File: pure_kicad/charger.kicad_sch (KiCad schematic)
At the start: 43 parts, among them J1 XT60M, J2 XT60M, Q1 Q_NMOS_DGS, Q2 Q_NMOS_DGS, Q3 Q_NMOS_DGS, Q4 Q_NMOS_DGS, U1 BQ25756ERRVR

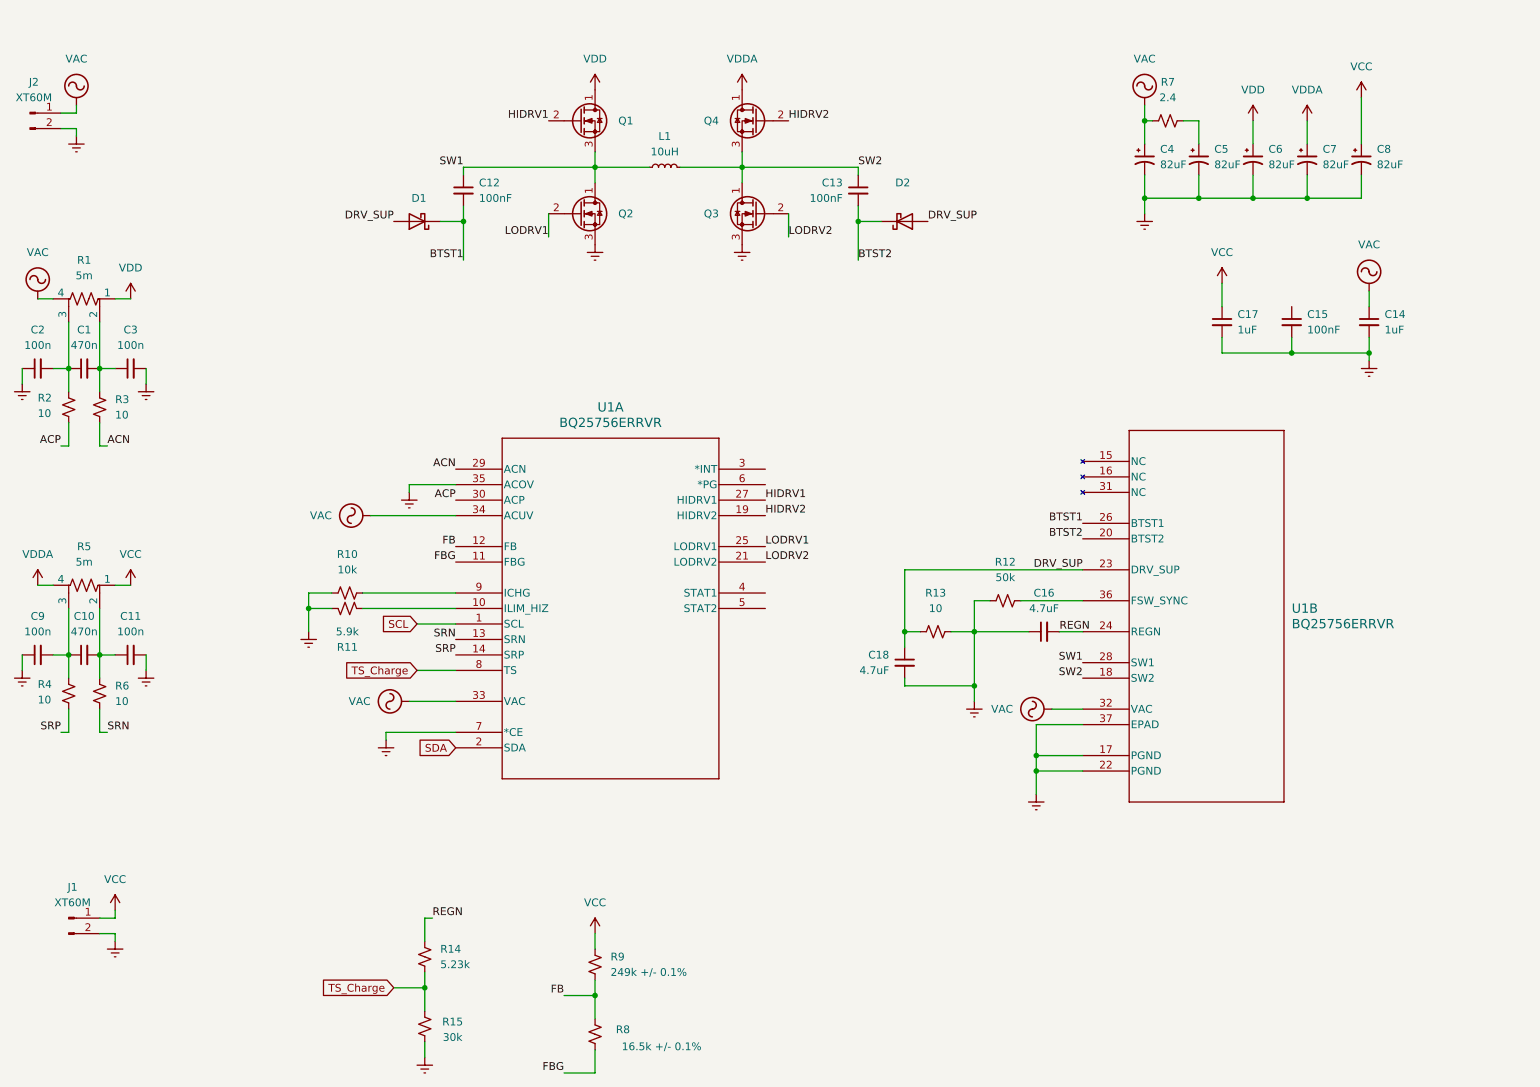
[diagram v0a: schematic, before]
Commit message: Assign parts, start layout
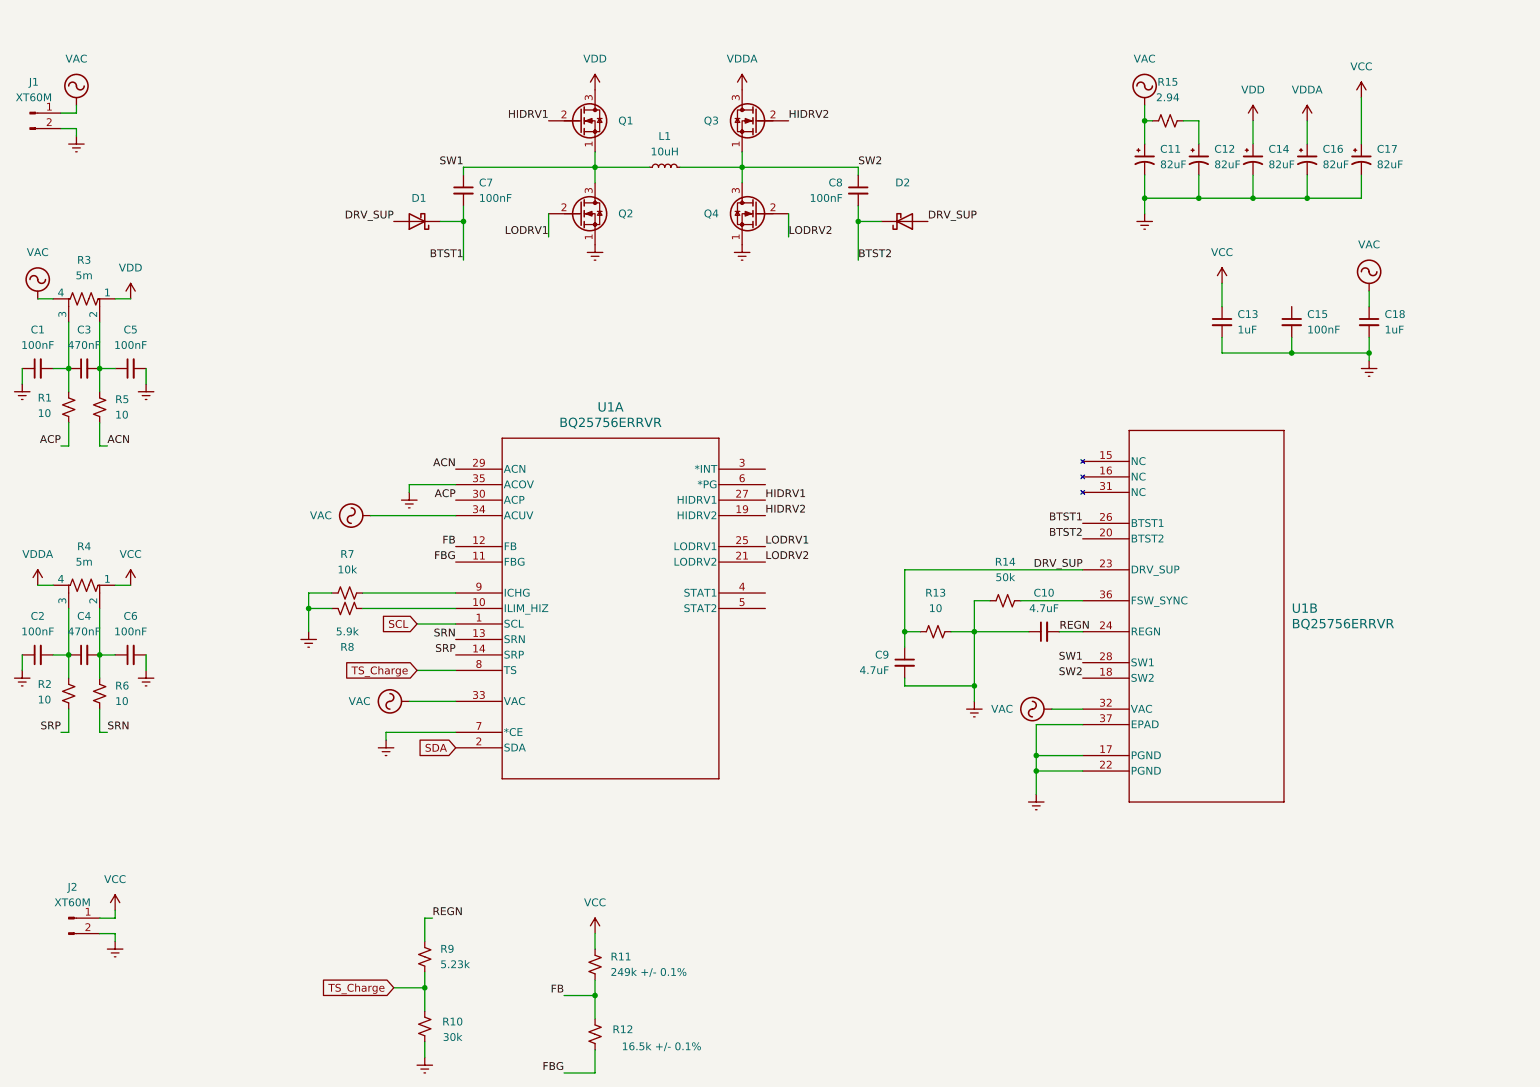
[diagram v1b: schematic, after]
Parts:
- C1: renamed from C2; value 100n -> 100nF; footprint Capacitor_SMD:C_0402_1005Metric_Pad0.74x0.62mm_HandSolder -> Capacitor_SMD:C_0603_1608Metric_Pad1.08x0.95mm_HandSolder
- C10: renamed from C16; footprint Capacitor_SMD:C_0402_1005Metric_Pad0.74x0.62mm_HandSolder -> Capacitor_SMD:C_0603_1608Metric_Pad1.08x0.95mm_HandSolder
- C11: renamed from C4; footprint (none) -> Capacitor_SMD:CP_Elec_10x14.3
- C12: renamed from C5; footprint (none) -> Capacitor_SMD:CP_Elec_10x14.3
- C13: renamed from C17; footprint (none) -> Capacitor_SMD:C_0603_1608Metric_Pad1.08x0.95mm_HandSolder
- C14: renamed from C6; footprint (none) -> Capacitor_SMD:CP_Elec_10x14.3
- C15: footprint (none) -> Capacitor_SMD:C_0603_1608Metric_Pad1.08x0.95mm_HandSolder
- C16: renamed from C7; footprint (none) -> Capacitor_SMD:CP_Elec_10x14.3
- C17: renamed from C8; footprint (none) -> Capacitor_SMD:CP_Elec_10x14.3
- C18: renamed from C14; footprint (none) -> Capacitor_SMD:C_0603_1608Metric_Pad1.08x0.95mm_HandSolder
- C2: renamed from C9; value 100n -> 100nF; footprint Capacitor_SMD:C_0402_1005Metric_Pad0.74x0.62mm_HandSolder -> Capacitor_SMD:C_0603_1608Metric_Pad1.08x0.95mm_HandSolder
- C3: renamed from C1; value 470n -> 470nF; footprint Capacitor_SMD:C_0402_1005Metric_Pad0.74x0.62mm_HandSolder -> Capacitor_SMD:C_0603_1608Metric_Pad1.08x0.95mm_HandSolder
- C4: renamed from C10; value 470n -> 470nF; footprint Capacitor_SMD:C_0402_1005Metric_Pad0.74x0.62mm_HandSolder -> Capacitor_SMD:C_0603_1608Metric_Pad1.08x0.95mm_HandSolder
- C5: renamed from C3; value 100n -> 100nF; footprint Capacitor_SMD:C_0402_1005Metric_Pad0.74x0.62mm_HandSolder -> Capacitor_SMD:C_0603_1608Metric_Pad1.08x0.95mm_HandSolder
- C6: renamed from C11; value 100n -> 100nF; footprint Capacitor_SMD:C_0402_1005Metric_Pad0.74x0.62mm_HandSolder -> Capacitor_SMD:C_0603_1608Metric_Pad1.08x0.95mm_HandSolder
- C7: renamed from C12; footprint (none) -> Capacitor_SMD:C_0603_1608Metric_Pad1.08x0.95mm_HandSolder
- C8: renamed from C13; footprint (none) -> Capacitor_SMD:C_0603_1608Metric_Pad1.08x0.95mm_HandSolder
- C9: renamed from C18; footprint Capacitor_SMD:C_0402_1005Metric_Pad0.74x0.62mm_HandSolder -> Capacitor_SMD:C_0603_1608Metric_Pad1.08x0.95mm_HandSolder
- D1, D2: footprint (none) -> Diode_SMD:D_SMA_Handsoldering
- L1: footprint (none) -> cyberec:IND-SMD_L13.5-W12.6
- Q1, Q2: footprint (none) -> cyberec:DFN-8_L3.0-W3.0-P0.65-BL-4; symbol Transistor_FET:Q_NMOS_DGS -> Transistor_FET:Q_NMOS_SGD
- Q3: renamed from Q4; footprint (none) -> cyberec:DFN-8_L3.0-W3.0-P0.65-BL-4; symbol Transistor_FET:Q_NMOS_DGS -> Transistor_FET:Q_NMOS_SGD
- Q4: renamed from Q3; footprint (none) -> cyberec:DFN-8_L3.0-W3.0-P0.65-BL-4; symbol Transistor_FET:Q_NMOS_DGS -> Transistor_FET:Q_NMOS_SGD
- R1: renamed from R2; footprint Resistor_SMD:R_0402_1005Metric_Pad0.72x0.64mm_HandSolder -> Resistor_SMD:R_0603_1608Metric_Pad0.98x0.95mm_HandSolder
- R10: renamed from R15; footprint Resistor_SMD:R_0402_1005Metric_Pad0.72x0.64mm_HandSolder -> Resistor_SMD:R_0603_1608Metric_Pad0.98x0.95mm_HandSolder
- R11: renamed from R9; footprint Resistor_SMD:R_0402_1005Metric_Pad0.72x0.64mm_HandSolder -> Resistor_SMD:R_0603_1608Metric_Pad0.98x0.95mm_HandSolder
- R12: renamed from R8; footprint Resistor_SMD:R_0402_1005Metric_Pad0.72x0.64mm_HandSolder -> Resistor_SMD:R_0603_1608Metric_Pad0.98x0.95mm_HandSolder
- R13, R6: footprint Resistor_SMD:R_0402_1005Metric_Pad0.72x0.64mm_HandSolder -> Resistor_SMD:R_0603_1608Metric_Pad0.98x0.95mm_HandSolder
- R15: renamed from R7; value 2.4 -> 2.94; footprint (none) -> Resistor_SMD:R_0603_1608Metric_Pad0.98x0.95mm_HandSolder
- R2: renamed from R4; footprint Resistor_SMD:R_0402_1005Metric_Pad0.72x0.64mm_HandSolder -> Resistor_SMD:R_0603_1608Metric_Pad0.98x0.95mm_HandSolder
- R3: renamed from R1; footprint (none) -> cyberec:R1206-sense-handsolder
- R4: renamed from R5; footprint (none) -> cyberec:R1206-sense-handsolder
- R5: renamed from R3; footprint Resistor_SMD:R_0402_1005Metric_Pad0.72x0.64mm_HandSolder -> Resistor_SMD:R_0603_1608Metric_Pad0.98x0.95mm_HandSolder
- R7: renamed from R10; footprint Resistor_SMD:R_0402_1005Metric_Pad0.72x0.64mm_HandSolder -> Resistor_SMD:R_0603_1608Metric_Pad0.98x0.95mm_HandSolder
- R8: renamed from R11; footprint Resistor_SMD:R_0402_1005Metric_Pad0.72x0.64mm_HandSolder -> Resistor_SMD:R_0603_1608Metric_Pad0.98x0.95mm_HandSolder
- R9: renamed from R14; footprint Resistor_SMD:R_0402_1005Metric_Pad0.72x0.64mm_HandSolder -> Resistor_SMD:R_0603_1608Metric_Pad0.98x0.95mm_HandSolder
- renumbered J2 to J1, J1 to J2, R12 to R14
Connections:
- net Earth: now also Q2.1 (S), Q4.1 (S); no longer Q2.3 (S), Q4.3 (S)
- net SW1: now also Q1.1 (S), Q2.3 (D); no longer Q1.3 (S), Q2.1 (D)
- net SW2: now also Q3.1 (S), Q4.3 (D); no longer Q3.3 (S), Q4.1 (D)
- net VDD: now also Q1.3 (D); no longer Q1.1 (D)
- net VDDA: now also Q3.3 (D); no longer Q3.1 (D)

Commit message: Layout starting to look alright
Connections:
- net VAC: now also C15.1
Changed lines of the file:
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@@
+	)
+	(junction
+		(at 256.54 63.5)
+		(diameter 0)
+		(color 0 0 0 0)
 	)
 	(junction
@@
 	(wire
 		(pts
+			(xy 256.54 63.5) (xy 256.54 64.77)
+		)
+		(stroke
+			(width 0)
+			(type default)
+		)
+	)
+	(wire
+		(pts
 			(xy 129.54 41.91) (xy 138.43 41.91)
 		)
@@
 	(wire
 		(pts
-			(xy 256.54 62.23) (xy 256.54 64.77)
+			(xy 256.54 62.23) (xy 256.54 63.5)
 		)
 		(stroke
@@
 	(wire
 		(pts
+			(xy 243.84 63.5) (xy 256.54 63.5)
+		)
+		(stroke
+			(width 0)
+			(type default)
+		)
+	)
+	(wire
+		(pts
 			(xy 40.64 74.93) (xy 43.18 74.93)
 		)
@@
 		)
 		(stroke
+			(width 0)
+			(type default)
+		)
+	)
+	(wire
+		(pts
+			(xy 243.84 64.77) (xy 243.84 63.5)
+		)
+		(stroke

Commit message: Import all the footprints, use project local 3d files
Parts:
- C1, C10, C13, C15, C18, C2, C3, C4, C5, C6, C7, C8, C9: footprint Capacitor_SMD:C_0603_1608Metric_Pad1.08x0.95mm_HandSolder -> cyberec:C_0603_1608Metric_Pad1.08x0.95mm_HandSolder
- C11, C12, C14, C16, C17: footprint Capacitor_SMD:CP_Elec_10x14.3 -> cyberec:CP_Elec_10x14.3
- D1, D2: footprint Diode_SMD:D_SMA_Handsoldering -> cyberec:D_SMA_Handsoldering
- J1, J2: footprint Connector_AMASS:AMASS_XT60-M_1x02_P7.20mm_Vertical -> cyberec:AMASS_XT60-M_1x02_P7.20mm_Vertical
- R1, R10, R11, R12, R13, R15, R2, R5, R6, R7, R8, R9: footprint Resistor_SMD:R_0603_1608Metric_Pad0.98x0.95mm_HandSolder -> cyberec:R_0603_1608Metric_Pad0.98x0.95mm_HandSolder
- R14: footprint Resistor_SMD:R_0402_1005Metric_Pad0.72x0.64mm_HandSolder -> cyberec:R_0402_1005Metric_Pad0.72x0.64mm_HandSolder
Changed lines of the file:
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@@
 			)
 		)
-		(property "Footprint" "Resistor_SMD:R_0603_1608Metric_Pad0.98x0.95mm_HandSolder"
+		(property "Footprint" "cyberec:R_0603_1608Metric_Pad0.98x0.95mm_HandSolder"
 			(at 185.42 118.11 0)
 			(effects
@@
 			)
 		)
-		(property "Footprint" "Capacitor_SMD:C_0603_1608Metric_Pad1.08x0.95mm_HandSolder"
+		(property "Footprint" "cyberec:C_0603_1608Metric_Pad1.08x0.95mm_HandSolder"
 			(at 38.1 121.92 0)
 			(effects
@@
 			)
 		)
-		(property "Footprint" "Capacitor_SMD:CP_Elec_10x14.3"
+		(property "Footprint" "cyberec:CP_Elec_10x14.3"
 			(at 246.38 40.64 0)
 			(effects
@@
 			)
 		)
-		(property "Footprint" "Diode_SMD:D_SMA_Handsoldering"
+		(property "Footprint" "cyberec:D_SMA_Handsoldering"
 			(at 100.33 50.8 0)
 			(effects
@@
 			)
 		)
-		(property "Footprint" "Capacitor_SMD:C_0603_1608Metric_Pad1.08x0.95mm_HandSolder"
+		(property "Footprint" "cyberec:C_0603_1608Metric_Pad1.08x0.95mm_HandSolder"
 			(at 107.95 45.72 0)
 			(effects
@@
 			)
 		)
-		(property "Footprint" "Resistor_SMD:R_0603_1608Metric_Pad0.98x0.95mm_HandSolder"
+		(property "Footprint" "cyberec:R_0603_1608Metric_Pad0.98x0.95mm_HandSolder"
 			(at 43.18 81.28 0)
 			(effects
@@
 			)
 		)
-		(property "Footprint" "Capacitor_SMD:CP_Elec_10x14.3"
+		(property "Footprint" "cyberec:CP_Elec_10x14.3"
 			(at 219.71 40.64 0)
 			(effects
@@
 			)
 		)
-		(property "Footprint" "Capacitor_SMD:CP_Elec_10x14.3"
+		(property "Footprint" "cyberec:CP_Elec_10x14.3"
 			(at 237.49 40.64 0)
 			(effects
@@
 			)
 		)
-		(property "Footprint" "Resistor_SMD:R_0603_1608Metric_Pad0.98x0.95mm_HandSolder"
+		(property "Footprint" "cyberec:R_0603_1608Metric_Pad0.98x0.95mm_HandSolder"
 			(at 48.26 128.27 0)
 			(effects
@@
 			)
 		)
-		(property "Footprint" "Capacitor_SMD:C_0603_1608Metric_Pad1.08x0.95mm_HandSolder"
+		(property "Footprint" "cyberec:C_0603_1608Metric_Pad1.08x0.95mm_HandSolder"
 			(at 180.34 123.19 0)
 			(effects
@@
 			)
 		)
-		(property "Footprint" "Resistor_SMD:R_0603_1608Metric_Pad0.98x0.95mm_HandSolder"
+		(property "Footprint" "cyberec:R_0603_1608Metric_Pad0.98x0.95mm_HandSolder"
 			(at 129.54 184.15 0)
 			(effects
@@
 			)
 		)
-		(property "Footprint" "Resistor_SMD:R_0603_1608Metric_Pad0.98x0.95mm_HandSolder"
+		(property "Footprint" "cyberec:R_0603_1608Metric_Pad0.98x0.95mm_HandSolder"
 			(at 101.6 182.88 0)
 			(effects
@@
 			)
 		)
-		(property "Footprint" "Connector_AMASS:AMASS_XT60-M_1x02_P7.20mm_Vertical"
+		(property "Footprint" "cyberec:AMASS_XT60-M_1x02_P7.20mm_Vertical"
 			(at 36.83 33.02 0)
 			(effects
@@
 			)
 		)
-		(property "Footprint" "Resistor_SMD:R_0603_1608Metric_Pad0.98x0.95mm_HandSolder"
+		(property "Footprint" "cyberec:R_0603_1608Metric_Pad0.98x0.95mm_HandSolder"
 			(at 223.52 34.29 0)
 			(effects
@@
 			)
 		)
-		(property "Footprint" "Capacitor_SMD:C_0603_1608Metric_Pad1.08x0.95mm_HandSolder"
+		(property "Footprint" "cyberec:C_0603_1608Metric_Pad1.08x0.95mm_HandSolder"
 			(at 45.72 121.92 0)
 			(effects
@@
 			)
 		)
-		(property "Footprint" "Capacitor_SMD:CP_Elec_10x14.3"
+		(property "Footprint" "cyberec:CP_Elec_10x14.3"
 			(at 228.6 40.64 0)
 			(effects
@@
 			)
 		)
-		(property "Footprint" "Resistor_SMD:R_0603_1608Metric_Pad0.98x0.95mm_HandSolder"
+		(property "Footprint" "cyberec:R_0603_1608Metric_Pad0.98x0.95mm_HandSolder"
 			(at 88.9 111.76 0)
 			(effects
@@
 			)
 		)
-		(property "Footprint" "Capacitor_SMD:CP_Elec_10x14.3"
+		(property "Footprint" "cyberec:CP_Elec_10x14.3"
 			(at 255.27 40.64 0)
 			(effects
@@
 			)
 		)
-		(property "Footprint" "Resistor_SMD:R_0402_1005Metric_Pad0.72x0.64mm_HandSolder"
+		(property "Footprint" "cyberec:R_0402_1005Metric_Pad0.72x0.64mm_HandSolder"
 			(at 196.85 113.03 0)
 			(effects
@@
 			)
 		)
-		(property "Footprint" "Capacitor_SMD:C_0603_1608Metric_Pad1.08x0.95mm_HandSolder"
+		(property "Footprint" "cyberec:C_0603_1608Metric_Pad1.08x0.95mm_HandSolder"
 			(at 232.41 67.31 0)
 			(effects
@@
 			)
 		)
-		(property "Footprint" "Capacitor_SMD:C_0603_1608Metric_Pad1.08x0.95mm_HandSolder"
+		(property "Footprint" "cyberec:C_0603_1608Metric_Pad1.08x0.95mm_HandSolder"
 			(at 53.34 121.92 0)
 			(effects
@@
 			)
 		)
-		(property "Footprint" "Capacitor_SMD:C_0603_1608Metric_Pad1.08x0.95mm_HandSolder"
+		(property "Footprint" "cyberec:C_0603_1608Metric_Pad1.08x0.95mm_HandSolder"
 			(at 45.72 74.93 0)
 			(effects
@@
 			)
 		)
-		(property "Footprint" "Capacitor_SMD:C_0603_1608Metric_Pad1.08x0.95mm_HandSolder"
+		(property "Footprint" "cyberec:C_0603_1608Metric_Pad1.08x0.95mm_HandSolder"
 			(at 172.72 45.72 0)
 			(effects
@@
 			)
 		)
-		(property "Footprint" "Resistor_SMD:R_0603_1608Metric_Pad0.98x0.95mm_HandSolder"
+		(property "Footprint" "cyberec:R_0603_1608Metric_Pad0.98x0.95mm_HandSolder"
 			(at 88.9 114.3 0)
 			(effects
@@
 			)
 		)
-		(property "Footprint" "Capacitor_SMD:C_0603_1608Metric_Pad1.08x0.95mm_HandSolder"
+		(property "Footprint" "cyberec:C_0603_1608Metric_Pad1.08x0.95mm_HandSolder"
 			(at 53.34 74.93 0)
 			(effects
@@
 			)
 		)
-		(property "Footprint" "Resistor_SMD:R_0603_1608Metric_Pad0.98x0.95mm_HandSolder"
+		(property "Footprint" "cyberec:R_0603_1608Metric_Pad0.98x0.95mm_HandSolder"
 			(at 48.26 81.28 0)
 			(effects
@@
 			)
 		)
-		(property "Footprint" "Capacitor_SMD:C_0603_1608Metric_Pad1.08x0.95mm_HandSolder"
+		(property "Footprint" "cyberec:C_0603_1608Metric_Pad1.08x0.95mm_HandSolder"
 			(at 203.2 118.11 0)
 			(effects
@@
 			)
 		)
-		(property "Footprint" "Resistor_SMD:R_0603_1608Metric_Pad0.98x0.95mm_HandSolder"
+		(property "Footprint" "cyberec:R_0603_1608Metric_Pad0.98x0.95mm_HandSolder"
 			(at 101.6 171.45 0)
 			(effects
@@
 			)
 		)
-		(property "Footprint" "Diode_SMD:D_SMA_Handsoldering"
+		(property "Footprint" "cyberec:D_SMA_Handsoldering"
 			(at 180.34 50.8 0)
 			(effects
@@
 			)
 		)
-		(property "Footprint" "Capacitor_SMD:C_0603_1608Metric_Pad1.08x0.95mm_HandSolder"
+		(property "Footprint" "cyberec:C_0603_1608Metric_Pad1.08x0.95mm_HandSolder"
 			(at 256.54 67.31 0)
 			(effects
@@
 			)
 		)
-		(property "Footprint" "Capacitor_SMD:C_0603_1608Metric_Pad1.08x0.95mm_HandSolder"
+		(property "Footprint" "cyberec:C_0603_1608Metric_Pad1.08x0.95mm_HandSolder"
 			(at 38.1 74.93 0)
 			(effects
@@
 			)
 		)
-		(property "Footprint" "Capacitor_SMD:C_0603_1608Metric_Pad1.08x0.95mm_HandSolder"
+		(property "Footprint" "cyberec:C_0603_1608Metric_Pad1.08x0.95mm_HandSolder"
 			(at 243.84 67.31 0)
 			(effects
@@
 			)
 		)
-		(property "Footprint" "Connector_AMASS:AMASS_XT60-M_1x02_P7.20mm_Vertical"
+		(property "Footprint" "cyberec:AMASS_XT60-M_1x02_P7.20mm_Vertical"
 			(at 43.18 165.1 0)
 			(effects
@@
 			)
 		)
-		(property "Footprint" "Resistor_SMD:R_0603_1608Metric_Pad0.98x0.95mm_HandSolder"
+		(property "Footprint" "cyberec:R_0603_1608Metric_Pad0.98x0.95mm_HandSolder"
 			(at 129.54 172.72 0)
 			(effects
@@
 			)
 		)
-		(property "Footprint" "Resistor_SMD:R_0603_1608Metric_Pad0.98x0.95mm_HandSolder"
+		(property "Footprint" "cyberec:R_0603_1608Metric_Pad0.98x0.95mm_HandSolder"
 			(at 43.18 128.27 0)
 			(effects

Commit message: Do most top side zones
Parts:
- D1, D2: value D_Schottky -> PMEG2010BELD; footprint cyberec:D_SMA_Handsoldering -> cyberec:D_SOD-882D
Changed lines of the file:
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@@
 			)
 		)
-		(property "Value" "D_Schottky"
+		(property "Value" "PMEG2010BELD"
 			(at 100.6475 46.99 0)
 			(effects
@@
 			)
 		)
-		(property "Footprint" "cyberec:D_SMA_Handsoldering"
+		(property "Footprint" "cyberec:D_SOD-882D"
 			(at 100.33 50.8 0)
 			(effects
@@
 			)
 		)
-		(property "Value" "D_Schottky"
+		(property "Value" "PMEG2010BELD"
 			(at 180.0225 46.99 0)
 			(effects
@@
 			)
 		)
-		(property "Footprint" "cyberec:D_SMA_Handsoldering"
+		(property "Footprint" "cyberec:D_SOD-882D"
 			(at 180.34 50.8 0)
 			(effects

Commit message: It seems that the charger needs to move.
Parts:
- J1: value XT60M -> XT30M; footprint cyberec:AMASS_XT60-M_1x02_P7.20mm_Vertical -> cyberec:AMASS_XT30U-M_1x02_P5.0mm_Vertical
- J2: value XT60M -> XT30F; footprint cyberec:AMASS_XT60-M_1x02_P7.20mm_Vertical -> cyberec:AMASS_XT30U-F_1x02_P5.0mm_Vertical
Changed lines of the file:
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@@
 			)
 		)
-		(property "Value" "XT60M"
+		(property "Value" "XT30M"
 			(at 37.465 30.48 0)
 			(effects
@@
 			)
 		)
-		(property "Footprint" "cyberec:AMASS_XT60-M_1x02_P7.20mm_Vertical"
+		(property "Footprint" "cyberec:AMASS_XT30U-M_1x02_P5.0mm_Vertical"
 			(at 36.83 33.02 0)
 			(effects
@@
 			)
 		)
-		(property "Value" "XT60M"
+		(property "Value" "XT30F"
 			(at 43.815 162.56 0)
 			(effects
@@
 			)
 		)
-		(property "Footprint" "cyberec:AMASS_XT60-M_1x02_P7.20mm_Vertical"
+		(property "Footprint" "cyberec:AMASS_XT30U-F_1x02_P5.0mm_Vertical"
 			(at 43.18 165.1 0)
 			(effects
